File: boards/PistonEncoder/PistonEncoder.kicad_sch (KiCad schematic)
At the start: 26 parts, among them J1 ISP, J2 PedalExt, J3 LED_Pwr, J4 LEDs1, J5 LEDs2, J6 Pistons1, J7 Pistons2, J8 BoardCon, U1 ATmega48-20P, U2 ULN2803A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

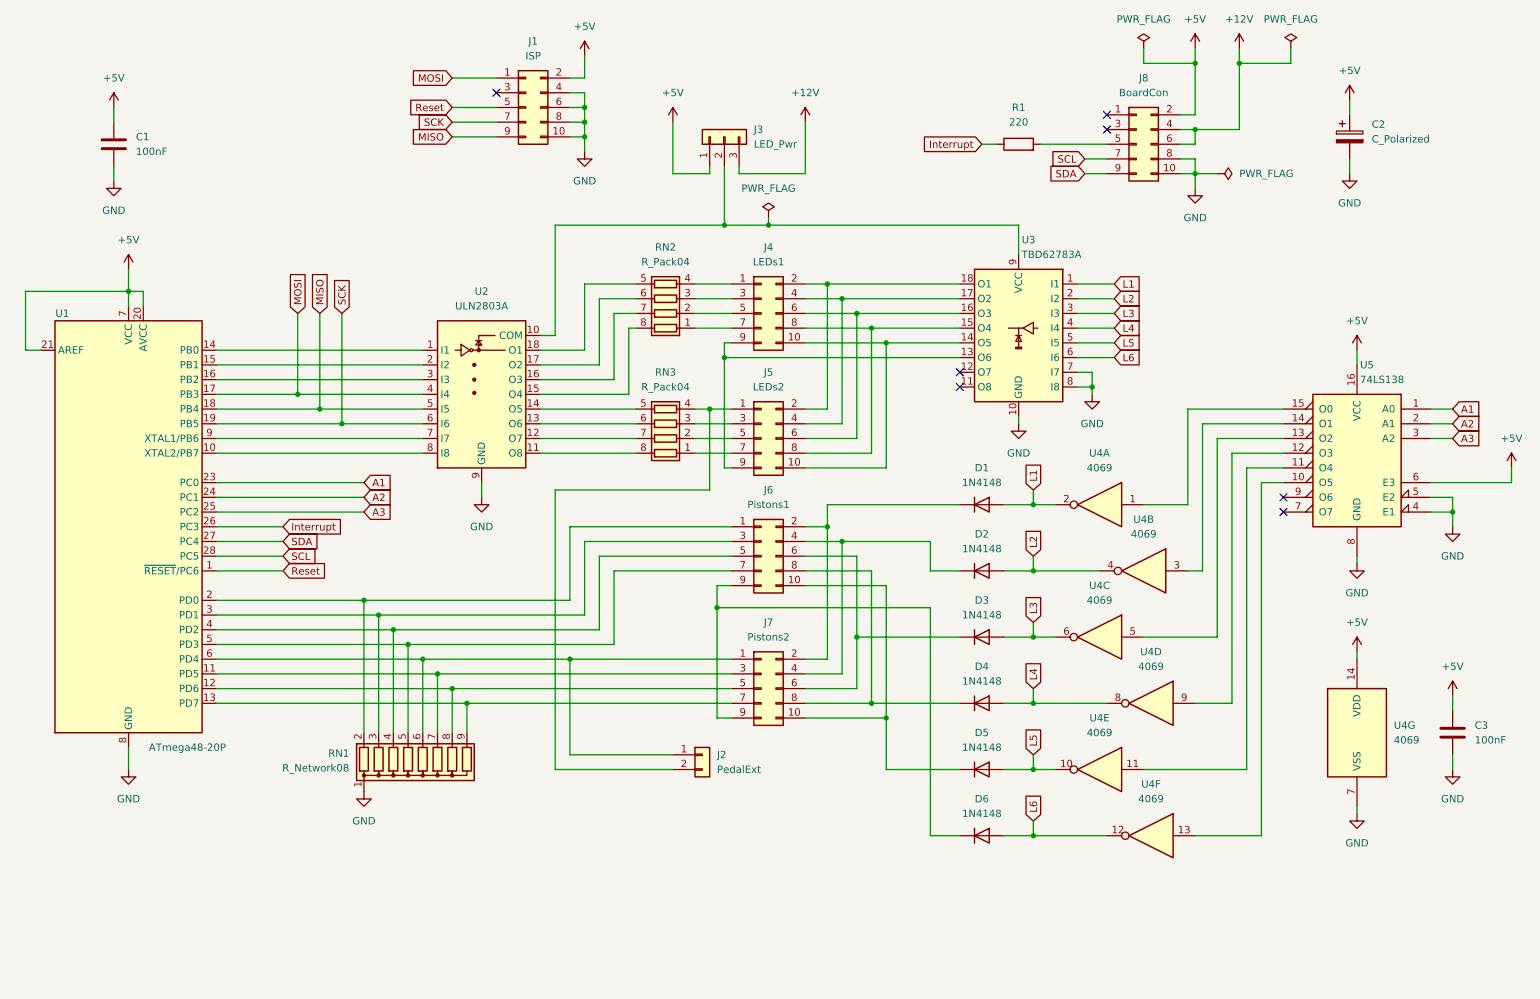
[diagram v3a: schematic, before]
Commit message: PCB layout for keyboard scanner and piston encoder
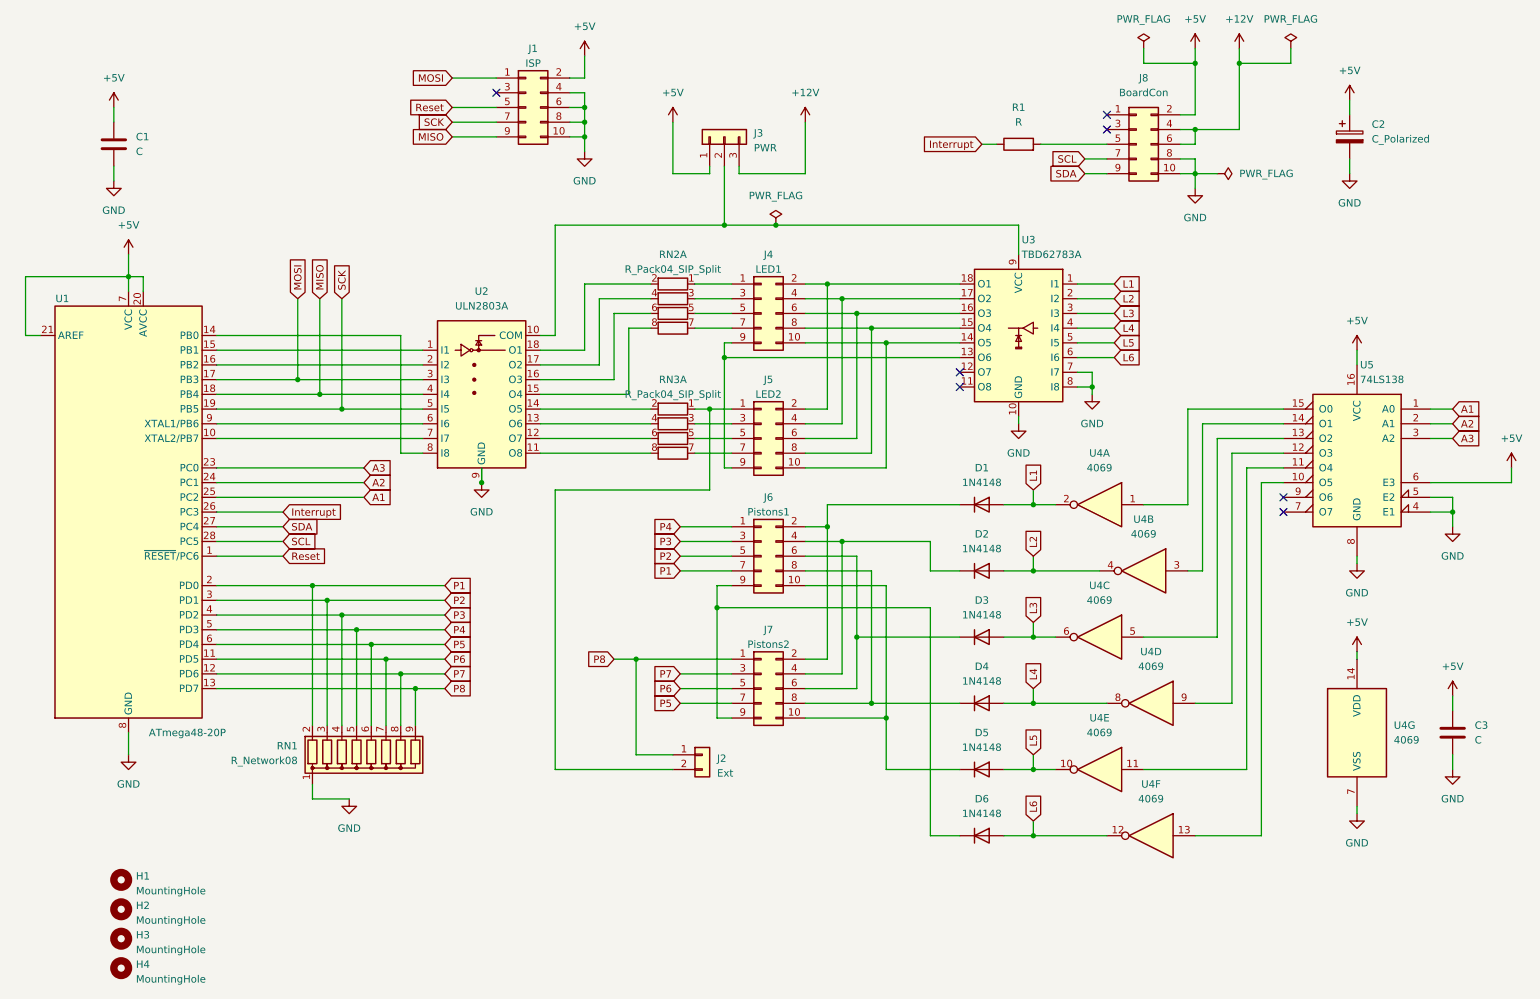
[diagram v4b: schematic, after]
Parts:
- removed RN2, RN3: R_Pack04, Resistor_THT:R_Array_SIP8, symbol Device:R_Pack04
- added H1, H2, H3, H4: MountingHole, MountingHole:MountingHole_3.2mm_M3, symbol Mechanical:MountingHole
- added RN2, RN3: R_Pack04_SIP_Split, Resistor_THT:R_Array_SIP8, symbol Device:R_Pack04_SIP_Split
- C1: value 100nF -> C; footprint Capacitor_THT:C_Disc_D7.5mm_W2.5mm_P5.00mm -> Capacitor_THT:C_Disc_D4.3mm_W1.9mm_P5.00mm
- C2: footprint Capacitor_THT:CP_Radial_D10.0mm_P5.00mm -> Capacitor_THT:C_Radial_D6.3mm_H7.0mm_P2.50mm
- C3: value 100nF -> C; footprint Capacitor_THT:C_Radial_D6.3mm_H11.0mm_P2.50mm -> Capacitor_THT:C_Disc_D4.3mm_W1.9mm_P5.00mm
- J2: value PedalExt -> Ext
- J3: value LED_Pwr -> PWR
- J4: value LEDs1 -> LED1
- J5: value LEDs2 -> LED2
- R1: value 220 -> R; footprint Resistor_THT:R_Axial_DIN0204_L3.6mm_D1.6mm_P2.54mm_Vertical -> Resistor_THT:R_Axial_DIN0204_L3.6mm_D1.6mm_P7.62mm_Horizontal
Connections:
- net A1: now also U1.25 (PC2); no longer U1.23 (PC0)
- net A3: now also U1.23 (PC0); no longer U1.25 (PC2)
- net MISO: now also U2.4 (I4); no longer U2.5 (I5)
- net MOSI: now also U2.3 (I3); no longer U2.4 (I4)
- net SCK: now also U2.5 (I5); no longer U2.6 (I6)
- net at J4.1 (Pin_1): now also RN2.1 (R1.1)
- net at J4.3 (Pin_3): now also RN2.3 (R2.1)
- net at J4.5 (Pin_5): now also RN2.5 (R3.1)
- net at J4.7 (Pin_7): now also RN2.7 (R4.1)
- net at U2.1 (I1): now also U1.15 (PB1); no longer U1.14 (PB0)
- net at U2.11 (O8): now also RN3.8 (R4.2)
- net at U2.12 (O7): now also RN3.6 (R3.2)
- net at U2.13 (O6): now also RN3.4 (R2.2)
- net at U2.14 (O5): now also RN3.2 (R1.2)
- net at U2.15 (O4): now also RN2.8 (R4.2)
- net at U2.16 (O3): now also RN2.6 (R3.2)
- net at U2.17 (O2): now also RN2.4 (R2.2)
- net at U2.18 (O1): now also RN2.2 (R1.2)
- net at U2.2 (I2): now also U1.16 (PB2); no longer U1.15 (PB1)
- net at U1.9 (XTAL1/PB6): now also U2.6 (I6); no longer U2.7 (I7)
- net at U1.10 (XTAL2/PB7): now also U2.7 (I7); no longer U2.8 (I8)
- net at J2.2 (Pin_2), J5.1 (Pin_1): now also RN3.1 (R1.1)
- net at J5.3 (Pin_3): now also RN3.3 (R2.1)
- net at J5.5 (Pin_5): now also RN3.5 (R3.1)
- net at J5.7 (Pin_7): now also RN3.7 (R4.1)
- net P6: now reaches RN1.7 (R6), U1.11 (PD5)
- net P6: now also J7.5 (Pin_5); no longer J7.3 (Pin_3)
- net P7: now reaches RN1.8 (R7), U1.12 (PD6)
- net P7: now also J7.3 (Pin_3); no longer J7.5 (Pin_5)
- net P8: now reaches RN1.9 (R8), U1.13 (PD7)
- net P8: now also J2.1 (Pin_1), J7.1 (Pin_1); no longer J7.7 (Pin_7)
- net P1: now reaches RN1.2 (R1), U1.2 (PD0)
- net P1: now also J6.7 (Pin_7); no longer J6.1 (Pin_1)
- net P2: now reaches RN1.3 (R2), U1.3 (PD1)
- net P2: now also J6.5 (Pin_5); no longer J6.3 (Pin_3)
- net P3: now reaches RN1.4 (R3), U1.4 (PD2)
- net P3: now also J6.3 (Pin_3); no longer J6.5 (Pin_5)
- net P4: now reaches RN1.5 (R4), U1.5 (PD3)
- net P4: now also J6.1 (Pin_1); no longer J6.7 (Pin_7)
- net P5: now reaches RN1.6 (R5), U1.6 (PD4)
- net P5: now also J7.7 (Pin_7); no longer J2.1 (Pin_1), J7.1 (Pin_1)
- new net: U1.14 (PB0), U2.8 (I8)

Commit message: Updated to KiCAD 8, fixed optocouplers for MIDI and added powersupplies
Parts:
- added C4: 100nF, Capacitor_THT:C_Disc_D4.3mm_W1.9mm_P5.00mm, symbol Device:C
- C1, C3: value C -> 100nF
- C2: value C_Polarized -> 10uF
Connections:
- net +5V: now also C4.1
- net GND: now also C4.2
- net LED_PWR: now reaches J3.2 (Pin_2), U2.10 (COM), U3.9 (VCC)

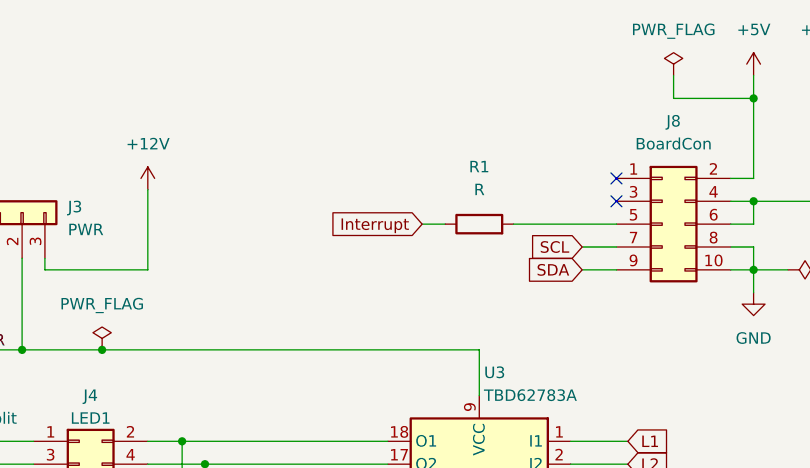
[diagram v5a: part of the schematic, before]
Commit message: Fixed interrupt line to use open collector, added pullups to I2C lines
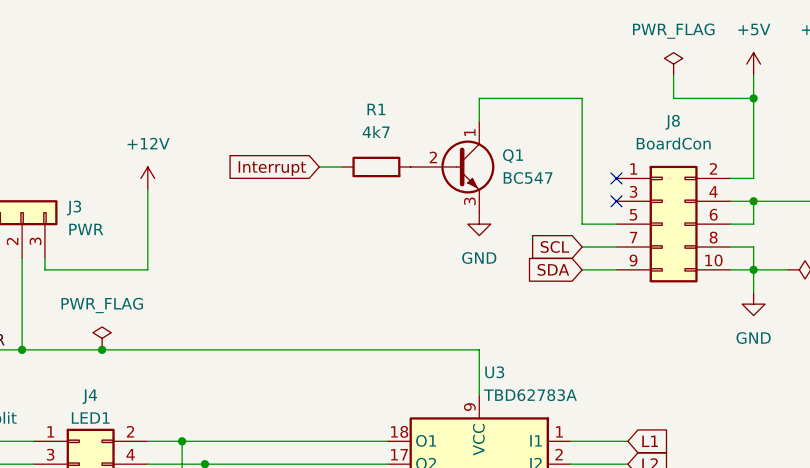
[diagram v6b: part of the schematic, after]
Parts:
- added Q1: BC547, Package_TO_SOT_THT:TO-92L_Inline_Wide, symbol Transistor_BJT:BC547
- R1: value R -> 4k7
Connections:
- net GND: now also Q1.3 (E)
- net at J8.5 (Pin_5): now also Q1.1 (C); no longer R1.2
- new net: Q1.2 (B), R1.2
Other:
- moved on the sheet: R1
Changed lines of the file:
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@@
 	(wire
 		(pts
+			(xy 193.04 26.67) (xy 204.47 26.67)
+		)
+		(stroke
+			(width 0)
+			(type default)
+		)
+	)
+	(wire
+		(pts
 			(xy 134.62 111.76) (xy 143.51 111.76)
 		)
@@
 	(wire
 		(pts
+			(xy 204.47 40.64) (xy 208.28 40.64)
+		)
+		(stroke
+			(width 0)
+			(type default)
+		)
+	)
+	(wire
+		(pts
 			(xy 182.88 148.59) (xy 170.18 148.59)
 		)
@@
 	(wire
 		(pts
-			(xy 196.85 40.64) (xy 208.28 40.64)
-		)
-		(stroke
-			(width 0)
-			(type default)
-		)
-	)
-	(wire
-		(pts
 			(xy 223.52 45.72) (xy 227.33 45.72)
 		)
@@
 	(wire
 		(pts
-			(xy 186.69 40.64) (xy 189.23 40.64)
+			(xy 175.26 34.29) (xy 177.8 34.29)
 		)
 		(stroke
@@
 	(wire
 		(pts
+			(xy 204.47 26.67) (xy 204.47 40.64)
+		)
+		(stroke
+			(width 0)
+			(type default)
+		)
+	)
+	(wire
+		(pts
 			(xy 54.61 121.92) (xy 76.2 121.92)
 		)
@@
 		)
 	)
+	(wire
+		(pts
+			(xy 193.04 29.21) (xy 193.04 26.67)
+		)
+		(stroke
+			(width 0)
+			(type default)
+		)
+	)
 	(label "LED_PWR"
 		(at 132.08 54.61 0)
@@
 	(global_label "Interrupt"
 		(shape input)
-		(at 186.69 40.64 180)
+		(at 175.26 34.29 180)
 		(fields_autoplaced yes)
 		(effects
@@
 		)
 		(property "Intersheetrefs" "${INTERSHEET_REFS}"
-			(at 176.1126 40.5606 0)
+			(at 164.6826 34.2106 0)
 			(effects
 				(font
@@
 	(symbol
 		(lib_id "Device:R")
-		(at 193.04 40.64 90)
+		(at 181.61 34.29 90)
 		(unit 1)
 		(exclude_from_sim no)
@@
 		(fields_autoplaced yes)
 		(property "Reference" "R1"
-			(at 193.04 34.29 90)
+			(at 181.61 27.94 90)
 			(effects
 				(font
@@
 			)
 		)
-		(property "Value" "R"
-			(at 193.04 36.83 90)
+		(property "Value" "4k7"
+			(at 181.61 30.48 90)
 			(effects
 				(font
@@
 		)
 		(property "Footprint" "Resistor_THT:R_Axial_DIN0204_L3.6mm_D1.6mm_P7.62mm_Horizontal"
-			(at 193.04 42.418 90)
+			(at 181.61 36.068 90)
 			(effects
 				(font
@@
 		)
 		(property "Datasheet" "~"
-			(at 193.04 40.64 0)
+			(at 181.61 34.29 0)
 			(effects
 				(font
@@
 		)
 		(property "Description" "Resistor"
-			(at 193.04 40.64 0)
+			(at 181.61 34.29 0)
 			(effects
 				(font
@@
 	)
 	(symbol
+		(lib_id "Transistor_BJT:BC547")
+		(at 190.5 34.29 0)
+		(unit 1)
+		(exclude_from_sim no)
+		(in_bom yes)
+		(on_board yes)
+		(dnp no)
+		(fields_autoplaced yes)
+		(property "Reference" "Q1"
+			(at 195.58 33.0199 0)
+			(effects
+				(font
+					(size 1.27 1.27)
+				)
+				(justify left)
+			)
+		)
+		(property "Value" "BC547"
+			(at 195.58 35.5599 0)
+			(effects
+				(font
+					(size 1.27 1.27)
+				)
+				(justify left)
+			)
+		)
+		(property "Footprint" "Package_TO_SOT_THT:TO-92L_Inline_Wide"
+			(at 195.58 36.195 0)
+			(effects
+				(font
+					(size 1.27 1.27)
+					(italic yes)
+				)
+				(justify left)
+				(hide yes)
+			)
+		)
+		(property "Datasheet" "https://www.onsemi.com/pub/Collateral/BC550-D.pdf"
+			(at 190.5 34.29 0)
+			(effects
+				(font
+					(size 1.27 1.27)
+				)
+				(justify left)
+				(hide yes)
+			)
+		)
+		(property "Description" "0.1A Ic, 45V Vce, Small Signal NPN Transistor, TO-92"
+			(at 190.5 34.29 0)
+			(effects
+				(font
+					(size 1.27 1.27)
+				)
+				(hide yes)
+			)
+		)
+		(pin "1"
+		)
+		(pin "2"
+		)
+		(pin "3"
+		)
+		(instances
+			(project "PistonEncoder"
+				(path "/78e9db5e-c1af-4070-a207-15eaf2d909bf"
+					(reference "Q1")
+					(unit 1)
+				)
+			)
+		)
+	)
+	(symbol
 		(lib_id "power:+5V")
 		(at 251.46 128.27 0)
@@
 					(unit 1)
 				)
+			)
+		)
+	)
+	(symbol
+		(lib_id "power:GND")
+		(at 193.04 39.37 0)
+		(unit 1)
+		(exclude_from_sim no)
+		(in_bom yes)
+		(on_board yes)
+		(dnp no)
+		(fields_autoplaced yes)
+		(property "Reference" "#PWR028"
+			(at 193.04 45.72 0)
+			(effects
+				(font
+					(size 1.27 1.27)
+				)
+				(hide yes)
+			)
+		)
+		(property "Value" "GND"
+			(at 193.04 44.45 0)
+			(effects
+				(font
+					(size 1.27 1.27)
+				)
+			)
+		)
+		(property "Footprint" ""
+			(at 193.04 39.37 0)
+			(effects
+				(font
+					(size 1.27 1.27)
+				)
+				(hide yes)
+			)
+		)
+		(property "Datasheet" ""
+			(at 193.04 39.37 0)
+			(effects
+				(font
+					(size 1.27 1.27)
+				)
+				(hide yes)
+			)
+		)
+		(property "Description" "Power symbol creates a global label with name \"GND\" , ground"
+			(at 193.04 39.37 0)
+			(effects
+				(font
+					(size 1.27 1.27)
+				)
+				(hide yes)
+			)
+		)
+		(pin "1"
+		)
+		(instances
+			(project "PistonEncoder"
+				(path "/78e9db5e-c1af-4070-a207-15eaf2d909bf"
+					(reference "#PWR028")
+					(unit 1)
+				)
